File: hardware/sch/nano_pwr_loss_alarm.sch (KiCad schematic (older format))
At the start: 15 parts, among them K301 RT314A12, Q301 BC547, Q302 BC557, Q303 BC547, Q304 SiA453EDJ

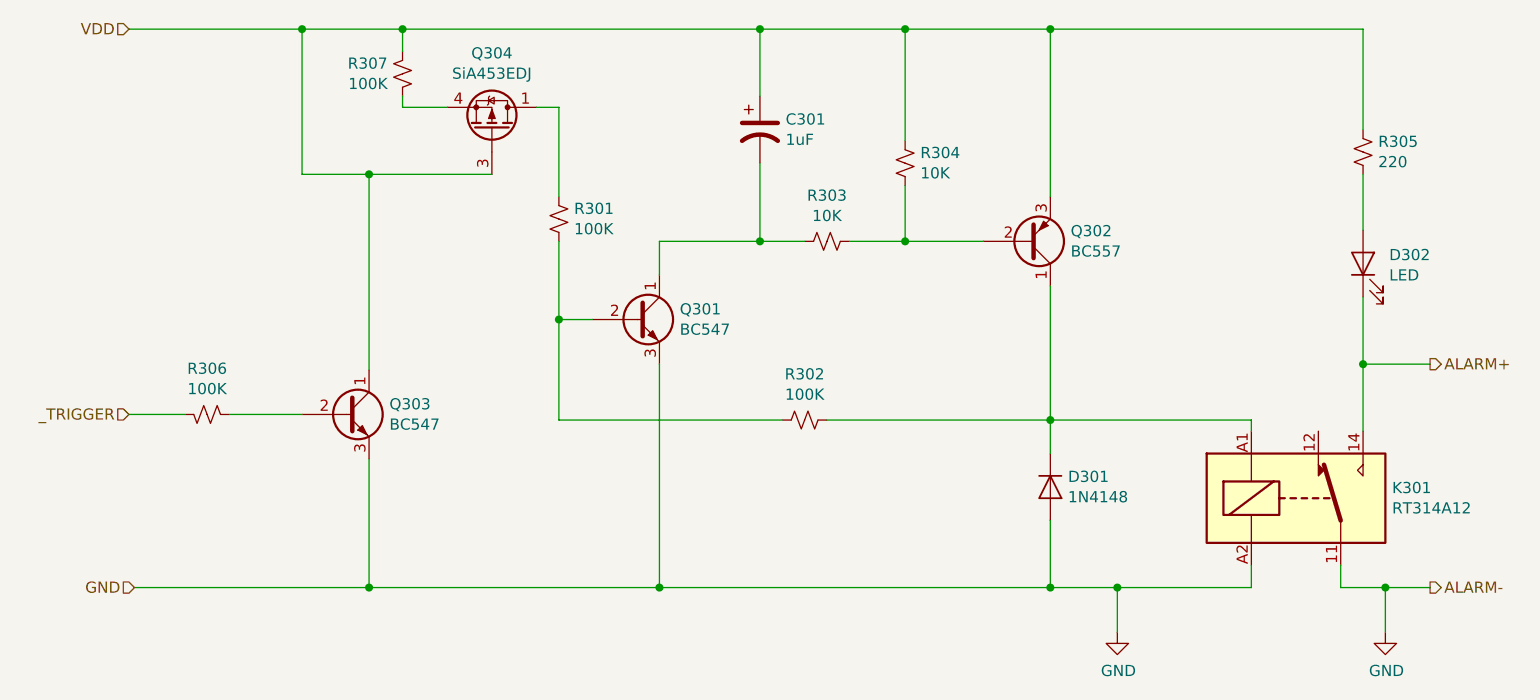
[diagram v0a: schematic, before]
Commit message: -Moved C104 to junction R104/R105 -Change I2C to 10K resistors -Moved R307 to VDD and G-Q304/C-Q303 junction -Updated K301 relay with G6EU -Remove D101 - LED -Added Analog User Controls (Buttons + PEEP/RR/TV Controls) -Added LCD PCF8574 module to I2C (Assume GND, VCC, SDA, SCL pin sequence) -Added schematic notes not to include alarm for controller prototyping.
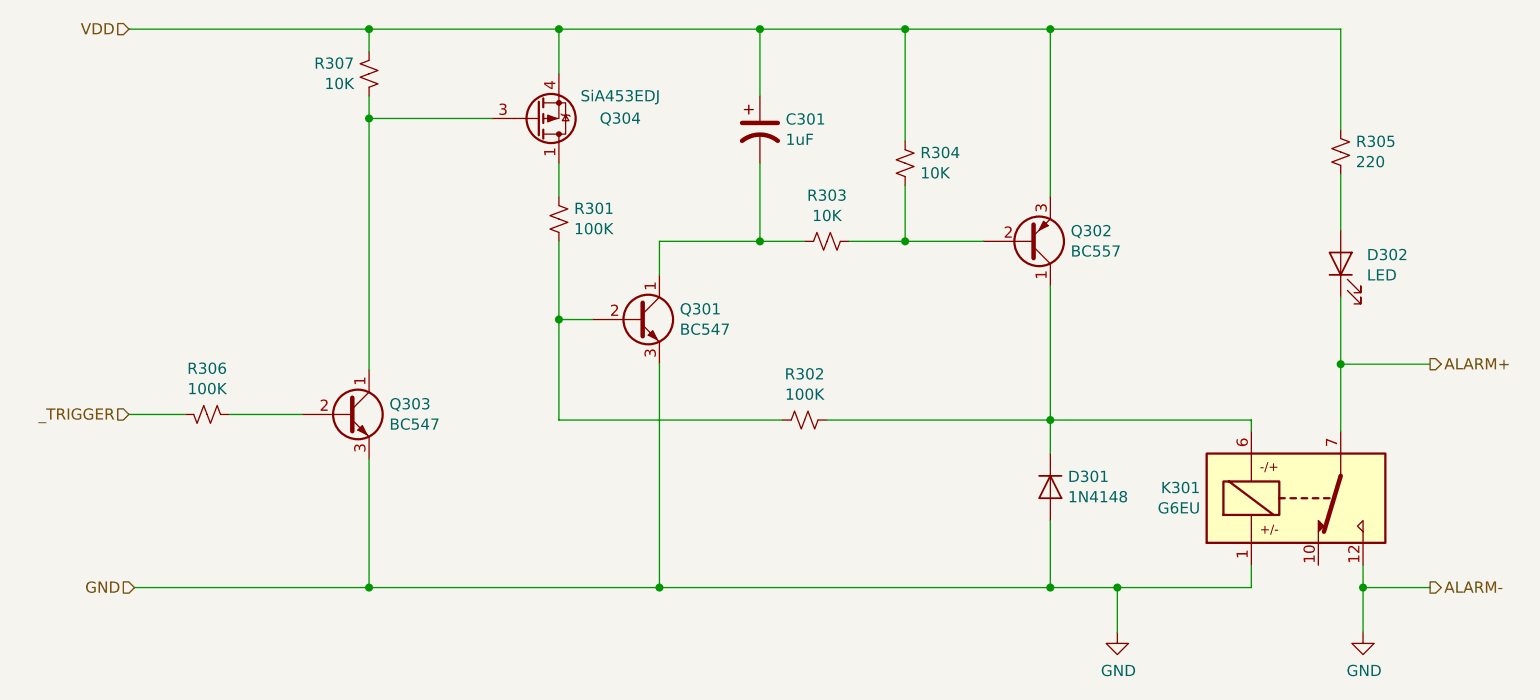
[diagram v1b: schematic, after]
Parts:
- removed K301: RT314A12, Relay_THT:Relay_SPDT_Schrack-RT1-16A-FormC_RM5mm, symbol Relay:RT314A12
- added K301: G6EU, Relay_THT:Relay_SPDT_Omron_G6E, symbol Relay:G6EU
- R307: value 100K -> 10K
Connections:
- net ALARM+: now also K301.7
- net GND: now also K301.1, K301.12
- net VDD: now also Q304.4 (S); no longer Q303.1 (C), Q304.3 (G)
- net at D301.1 (K), Q302.1 (C), R302.1: now also K301.6
- net at R307.1: now also Q303.1 (C), Q304.3 (G); no longer Q304.4 (S)
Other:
- moved on the sheet: D302, Q304, R305, R307
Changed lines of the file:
@@
 $Descr A4 11693 8268
 encoding utf-8
-Sheet 3 3
+Sheet 3 4
 Title "OpenSourceVentilator Controller"
 Date "Mar. 28 2020"
-Rev "1"
+Rev "1b"
 Comp "https://github.com/ermtl/Open-Source-Ventilator"
-Comment1 "Robbie Sharma"
+Comment1 "Drafting: Robbie Sharma"
 Comment2 ""
 Comment3 ""
@@
 L Device:R_Small_US R305
 U 1 1 5E877E6F
-P 8575 2675
-F 0 "R305" H 8643 2721 50  0000 L CNN
-F 1 "220" H 8643 2630 50  0000 L CNN
-F 2 "" H 8575 2675 50  0001 C CNN
-F 3 "~" H 8575 2675 50  0001 C CNN
-	1    8575 2675
+P 8475 2675
+F 0 "R305" H 8543 2721 50  0000 L CNN
+F 1 "220" H 8543 2630 50  0000 L CNN
+F 2 "" H 8475 2675 50  0001 C CNN
+F 3 "~" H 8475 2675 50  0001 C CNN
+	1    8475 2675
 	1    0    0    -1
 $EndComp
@@
 L Device:LED D302
 U 1 1 5E8784E9
-P 8575 3175
-F 0 "D302" V 8614 3058 50  0000 R CNN
-F 1 "LED" V 8523 3058 50  0000 R CNN
-F 2 "" H 8575 3175 50  0001 C CNN
-F 3 "~" H 8575 3175 50  0001 C CNN
-	1    8575 3175
+P 8475 3175
+F 0 "D302" V 8514 3058 50  0000 R CNN
+F 1 "LED" V 8423 3058 50  0000 R CNN
+F 2 "" H 8475 3175 50  0001 C CNN
+F 3 "~" H 8475 3175 50  0001 C CNN
+	1    8475 3175
 	0    -1   -1   0
 $EndComp
@@
 	-1   0    0    1
 $EndComp
-$Comp
-L Relay:RT314A12 K301
-U 1 1 5E87C70E
-P 8275 4225
-F 0 "K301" H 8705 4271 50  0000 L CNN
-F 1 "RT314A12" H 8705 4180 50  0000 L CNN
-F 2 "Relay_THT:Relay_SPDT_Schrack-RT1-16A-FormC_RM5mm" H 9825 4175 50  0001 C CNN
-F 3 "https://www.te.com/commerce/DocumentDelivery/DDEController?Action=srchrtrv&DocNm=RT1_bistable&DocType=DS&DocLang=English" H 8275 4225 50  0001 C CNN
-	1    8275 4225
-	1    0    0    -1
-$EndComp
 Wire Wire Line
 	5875 2725 5875 3075
@@
 	5875 3075 6075 3075
 Wire Wire Line
-	8575 2775 8575 3025
+	8475 2775 8475 3025
 Wire Wire Line
 	6525 2825 6525 3075
@@
 ALARM-
 Wire Wire Line
-	8575 2125 8575 2575
-Wire Wire Line
-	8475 4525 8475 4625
-Wire Wire Line
-	8475 4625 8675 4625
+	8475 2125 8475 2575
+Wire Wire Line
+	8575 4525 8575 4625
 $Comp
 L power:GND #PWR0302
 U 1 1 5E8867CF
-P 8675 4825
-F 0 "#PWR0302" H 8675 4575 50  0001 C CNN
-F 1 "GND" H 8680 4652 50  0000 C CNN
-F 2 "" H 8675 4825 50  0001 C CNN
-F 3 "" H 8675 4825 50  0001 C CNN
-	1    8675 4825
+P 8575 4825
+F 0 "#PWR0302" H 8575 4575 50  0001 C CNN
+F 1 "GND" H 8580 4652 50  0000 C CNN
+F 2 "" H 8575 4825 50  0001 C CNN
+F 3 "" H 8575 4825 50  0001 C CNN
+	1    8575 4825
 	1    0    0    -1
 $EndComp
@@
 	7475 4625 8075 4625
 Wire Wire Line
-	8675 4625 8675 4825
-Connection ~ 8675 4625
-Wire Wire Line
-	8675 4625 8875 4625
+	8575 4625 8575 4825
+Connection ~ 8575 4625
+Wire Wire Line
+	8575 4625 8875 4625
 Connection ~ 5425 4625
-Wire Wire Line
-	3050 2125 3825 2125
 $Comp
 L Transistor_BJT:BC547 Q303
@@
 $EndComp
 Wire Wire Line
-	6525 2125 7175 2125
-Wire Wire Line
-	8575 3325 8575 3625
-Wire Wire Line
-	8875 3625 8575 3625
-Connection ~ 8575 3625
-Wire Wire Line
-	8575 3625 8575 3925
-Wire Wire Line
-	7175 2125 8575 2125
-Connection ~ 3825 2125
+	8475 3325 8475 3625
+Wire Wire Line
+	8875 3625 8475 3625
+Connection ~ 8475 3625
+Wire Wire Line
+	8475 3625 8475 3925
 Connection ~ 5875 2125
 Wire Wire Line
-	3825 2775 4125 2775
-Connection ~ 4125 2775
-Wire Wire Line
-	4275 2475 4475 2475
-Wire Wire Line
-	4125 2775 4675 2775
-Wire Wire Line
-	4875 2475 4975 2475
-Wire Wire Line
-	4975 2475 4975 2875
-Wire Wire Line
 	4975 3075 4975 3425
-$Comp
-L Transistor_FET:SiA453EDJ Q304
-U 1 1 5E8BB916
-P 4675 2575
-F 0 "Q304" V 5017 2575 50  0000 C CNN
-F 1 "SiA453EDJ" V 4926 2575 50  0000 C CNN
-F 2 "Package_TO_SOT_SMD:Vishay_PowerPAK_SC70-6L_Single" H 4875 2500 50  0001 L CIN
-F 3 "http://www.vishay.com/docs/62864/sia453edj.pdf" V 4675 2575 50  0001 L CNN
-	1    4675 2575
-	0    1    -1   0
-$EndComp
 $Comp
 L Device:R_Small_US R306
@@
 $EndComp
 Wire Wire Line
-	3825 2125 3825 2775
-Wire Wire Line
 	3500 3850 3825 3850
 Wire Wire Line
 	3050 3850 3300 3850
-Wire Wire Line
-	3825 2125 4275 2125
 $Comp
 L Device:R_Small_US R307
 U 1 1 5E926BC7
-P 4275 2325
-F 0 "R307" H 4208 2279 50  0000 R CNN
-F 1 "100K" H 4208 2370 50  0000 R CNN
-F 2 "" H 4275 2325 50  0001 C CNN
-F 3 "~" H 4275 2325 50  0001 C CNN
-	1    4275 2325
+P 4125 2325
+F 0 "R307" H 4058 2279 50  0000 R CNN
+F 1 "10K" H 4058 2370 50  0000 R CNN
+F 2 "" H 4125 2325 50  0001 C CNN
+F 3 "~" H 4125 2325 50  0001 C CNN
+	1    4125 2325
 	1    0    0    1
 $EndComp
 Wire Wire Line
-	4275 2125 4275 2225
-Connection ~ 4275 2125
-Wire Wire Line
-	4275 2125 5875 2125
-Wire Wire Line
-	4275 2425 4275 2475
-Wire Wire Line
 	3075 4625 4125 4625
-Wire Wire Line
-	4125 2775 4125 3650
 Wire Wire Line
 	4125 4050 4125 4625
@@
 Wire Wire Line
 	4125 4625 5425 4625
+Wire Wire Line
+	4675 2525 4125 2525
+$Comp
+L Transistor_FET:SiA453EDJ Q304
+U 1 1 5E8BB916
+P 4875 2525
+F 0 "Q304" H 5250 2525 50  0000 C CNN
+F 1 "SiA453EDJ" H 5250 2425 50  0000 C CNN
+F 2 "Package_TO_SOT_SMD:Vishay_PowerPAK_SC70-6L_Single" H 5075 2450 50  0001 L CIN
+F 3 "http://www.vishay.com/docs/62864/sia453edj.pdf" V 4875 2525 50  0001 L CNN
+	1    4875 2525
+	1    0    0    1
+$EndComp
+Wire Wire Line
+	4975 2725 4975 2875
+Wire Wire Line
+	4975 2125 4975 2325
+Connection ~ 4975 2125
+Wire Wire Line
+	4975 2125 5875 2125
+Wire Wire Line
+	3050 2125 4125 2125
+Wire Wire Line
+	4125 2125 4125 2225
+Connection ~ 4125 2125
+Wire Wire Line
+	4125 2125 4975 2125
+Wire Wire Line
+	4125 2425 4125 2525
+Connection ~ 4125 2525
+Wire Wire Line
+	4125 2525 4125 3650
+$Comp
+L Relay:G6EU K301
+U 1 1 5EA9DD6B
+P 8275 4225
+F 0 "K301" H 7846 4179 50  0000 R CNN
+F 1 "G6EU" H 7846 4270 50  0000 R CNN
+F 2 "Relay_THT:Relay_SPDT_Omron_G6E" H 9405 4195 50  0001 C CNN
+F 3 "https://www.omron.com/ecb/products/pdf/en-g6e.pdf" H 8275 4225 50  0001 C CNN
+	1    8275 4225
+	1    0    0    1
+$EndComp
+Wire Wire Line
+	7175 2125 8475 2125
+Wire Wire Line
+	6525 2125 7175 2125
 $EndSCHEMATC
